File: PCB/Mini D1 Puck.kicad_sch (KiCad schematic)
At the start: 10 parts, among them M1 VI1, M2 VI2, M3 VI3, M4 VI4, Q1 2N2222, SW1 SW_SPDT

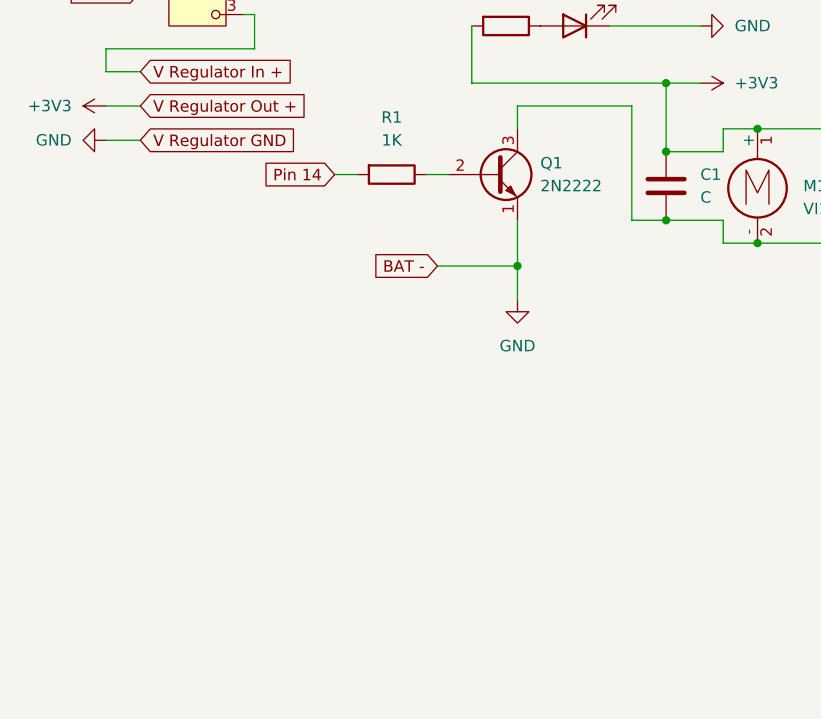
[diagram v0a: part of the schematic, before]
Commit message: Add voltage divider to schematic to measure battery level
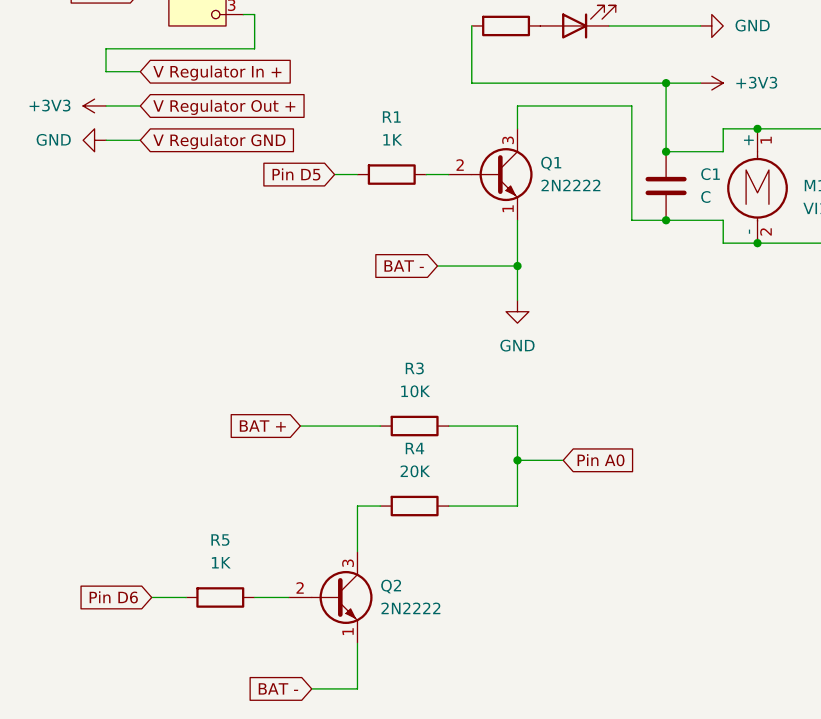
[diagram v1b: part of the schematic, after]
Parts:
- added Q2: 2N2222, symbol Transistor_BJT:Q_NPN_EBC
- added R3: 10K, symbol Device:R
- added R4: 20K, symbol Device:R
- added R5: 1K, symbol Device:R
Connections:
- net BAT +: now also R3.2
- net GND: now also Q2.1 (E)
- net Pin 14 renamed Pin D5
- new net: Q2.2 (B), R5.1
- new net: Q2.3 (C), R4.2
- new net Pin A0: R3.1, R4.1
- new net Pin D6: R5.2

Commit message: Ui WORK
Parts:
- C1: value C -> 200uF
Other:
- moved on the sheet: M1, M2, M3
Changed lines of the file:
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@@
-	)
-	(junction
-		(at 124.46 48.26)
-		(diameter 0)
-		(color 0 0 0 0)
-	)
-	(junction
-		(at 124.46 60.96)
-		(diameter 0)
-		(color 0 0 0 0)
 	)
 	(junction
@@
 	)
 	(junction
-		(at 99.06 48.26)
+		(at 125.73 60.96)
+		(diameter 0)
+		(color 0 0 0 0)
+	)
+	(junction
+		(at 114.3 60.96)
 		(diameter 0)
 		(color 0 0 0 0)
@@
 	)
 	(junction
-		(at 111.76 60.96)
+		(at 102.87 60.96)
 		(diameter 0)
 		(color 0 0 0 0)
 	)
 	(junction
-		(at 99.06 60.96)
+		(at 102.87 48.26)
+		(diameter 0)
+		(color 0 0 0 0)
+	)
+	(junction
+		(at 125.73 48.26)
 		(diameter 0)
 		(color 0 0 0 0)
@@
 	)
 	(junction
-		(at 111.76 48.26)
+		(at 114.3 48.26)
 		(diameter 0)
 		(color 0 0 0 0)
@@
 	(wire
 		(pts
+			(xy 102.87 60.96) (xy 114.3 60.96)
+		)
+		(stroke
+			(width 0)
+			(type default)
+		)
+	)
+	(wire
+		(pts
 			(xy 85.09 45.72) (xy 85.09 58.42)
 		)
@@
 	(wire
 		(pts
+			(xy 125.73 48.26) (xy 137.16 48.26)
+		)
+		(stroke
+			(width 0)
+			(type default)
+		)
+	)
+	(wire
+		(pts
 			(xy 72.39 81.28) (xy 72.39 85.09)
 		)
@@
 	(wire
 		(pts
-			(xy 111.76 60.96) (xy 124.46 60.96)
-		)
-		(stroke
-			(width 0)
-			(type default)
-		)
-	)
-	(wire
-		(pts
 			(xy 88.9 50.8) (xy 95.25 50.8)
 		)
@@
 	(wire
 		(pts
-			(xy 99.06 48.26) (xy 111.76 48.26)
+			(xy 114.3 48.26) (xy 125.73 48.26)
 		)
 		(stroke
@@
 	(wire
 		(pts
-			(xy 111.76 48.26) (xy 124.46 48.26)
-		)
-		(stroke
-			(width 0)
-			(type default)
-		)
-	)
-	(wire
-		(pts
 			(xy 54.61 110.49) (xy 49.53 110.49)
 		)
@@
 	(wire
 		(pts
-			(xy 124.46 60.96) (xy 137.16 60.96)
-		)
-		(stroke
-			(width 0)
-			(type default)
-		)
-	)
-	(wire
-		(pts
 			(xy 72.39 45.72) (xy 85.09 45.72)
 		)
@@
 	(wire
 		(pts
-			(xy 95.25 60.96) (xy 99.06 60.96)
+			(xy 95.25 60.96) (xy 102.87 60.96)
 		)
 		(stroke
@@
 	(wire
 		(pts
+			(xy 102.87 48.26) (xy 114.3 48.26)
+		)
+		(stroke
+			(width 0)
+			(type default)
+		)
+	)
+	(wire
+		(pts
 			(xy 26.67 39.37) (xy 26.67 41.91)
 		)
@@
 	(wire
 		(pts
+			(xy 125.73 60.96) (xy 137.16 60.96)
+		)
+		(stroke
+			(width 0)
+			(type default)
+		)
+	)
+	(wire
+		(pts
 			(xy 95.25 58.42) (xy 95.25 60.96)
 		)
@@
 	(wire
 		(pts
+			(xy 114.3 60.96) (xy 125.73 60.96)
+		)
+		(stroke
+			(width 0)
+			(type default)
+		)
+	)
+	(wire
+		(pts
 			(xy 64.77 81.28) (xy 72.39 81.28)
 		)
@@
 	(wire
 		(pts
-			(xy 124.46 48.26) (xy 137.16 48.26)
-		)
-		(stroke
-			(width 0)
-			(type default)
-		)
-	)
-	(wire
-		(pts
 			(xy 72.39 45.72) (xy 72.39 48.26)
 		)
@@
 	(wire
 		(pts
-			(xy 99.06 60.96) (xy 111.76 60.96)
-		)
-		(stroke
-			(width 0)
-			(type default)
-		)
-	)
-	(wire
-		(pts
 			(xy 82.55 36.83) (xy 92.71 36.83)
 		)
@@
 	(wire
 		(pts
-			(xy 95.25 48.26) (xy 99.06 48.26)
+			(xy 95.25 48.26) (xy 102.87 48.26)
 		)
 		(stroke
@@
 			)
 		)
-		(property "Value" "C"
+		(property "Value" "200uF"
 			(at 92.71 55.8799 0)
 			(effects
@@
 	(symbol
 		(lib_id "Motor:Motor_DC")
-		(at 111.76 53.34 0)
+		(at 114.3 53.34 0)
 		(unit 1)
 		(exclude_from_sim no)
@@
 		(fields_autoplaced yes)
 		(property "Reference" "M2"
-			(at 116.84 54.6099 0)
+			(at 119.38 54.6099 0)
 			(effects
 				(font
@@
 		)
 		(property "Value" "VI2"
-			(at 116.84 57.1499 0)
+			(at 119.38 57.1499 0)
 			(effects
 				(font
@@
 		)
 		(property "Footprint" ""
-			(at 111.76 55.626 0)
+			(at 114.3 55.626 0)
 			(effects
 				(font
@@
 		)
 		(property "Datasheet" "~"
-			(at 111.76 55.626 0)
+			(at 114.3 55.626 0)
 			(effects
 				(font
@@
 		)
 		(property "Description" "DC Motor"
-			(at 111.76 53.34 0)
+			(at 114.3 53.34 0)
 			(effects
 				(font
@@
 	(symbol
 		(lib_id "Motor:Motor_DC")
-		(at 124.46 53.34 0)
+		(at 125.73 53.34 0)
 		(unit 1)
 		(exclude_from_sim no)
@@
 		(fields_autoplaced yes)
 		(property "Reference" "M3"
-			(at 129.54 54.6099 0)
+			(at 130.81 54.6099 0)
 			(effects
 				(font
@@
 		)
 		(property "Value" "VI3"
-			(at 129.54 57.1499 0)
+			(at 130.81 57.1499 0)
 			(effects
 				(font
@@
 		)
 		(property "Footprint" ""
-			(at 124.46 55.626 0)
+			(at 125.73 55.626 0)
 			(effects
 				(font
@@
 		)
 		(property "Datasheet" "~"
-			(at 124.46 55.626 0)
+			(at 125.73 55.626 0)
 			(effects
 				(font
@@
 		)
 		(property "Description" "DC Motor"
-			(at 124.46 53.34 0)
+			(at 125.73 53.34 0)
 			(effects
 				(font
@@
 	(symbol
 		(lib_id "Motor:Motor_DC")
-		(at 99.06 53.34 0)
+		(at 102.87 53.34 0)
 		(unit 1)
 		(exclude_from_sim no)
@@
 		(fields_autoplaced yes)
 		(property "Reference" "M1"
-			(at 104.14 54.6099 0)
+			(at 107.95 54.6099 0)
 			(effects
 				(font
@@
 		)
 		(property "Value" "VI1"
-			(at 104.14 57.1499 0)
+			(at 107.95 57.1499 0)
 			(effects
 				(font
@@
 		)
 		(property "Footprint" ""
-			(at 99.06 55.626 0)
+			(at 102.87 55.626 0)
 			(effects
 				(font
@@
 		)
 		(property "Datasheet" "~"
-			(at 99.06 55.626 0)
+			(at 102.87 55.626 0)
 			(effects
 				(font
@@
 		)
 		(property "Description" "DC Motor"
-			(at 99.06 53.34 0)
-			(effects
-				(font
+			(at 102.87 53.34 0)
+			(effects
+				(font

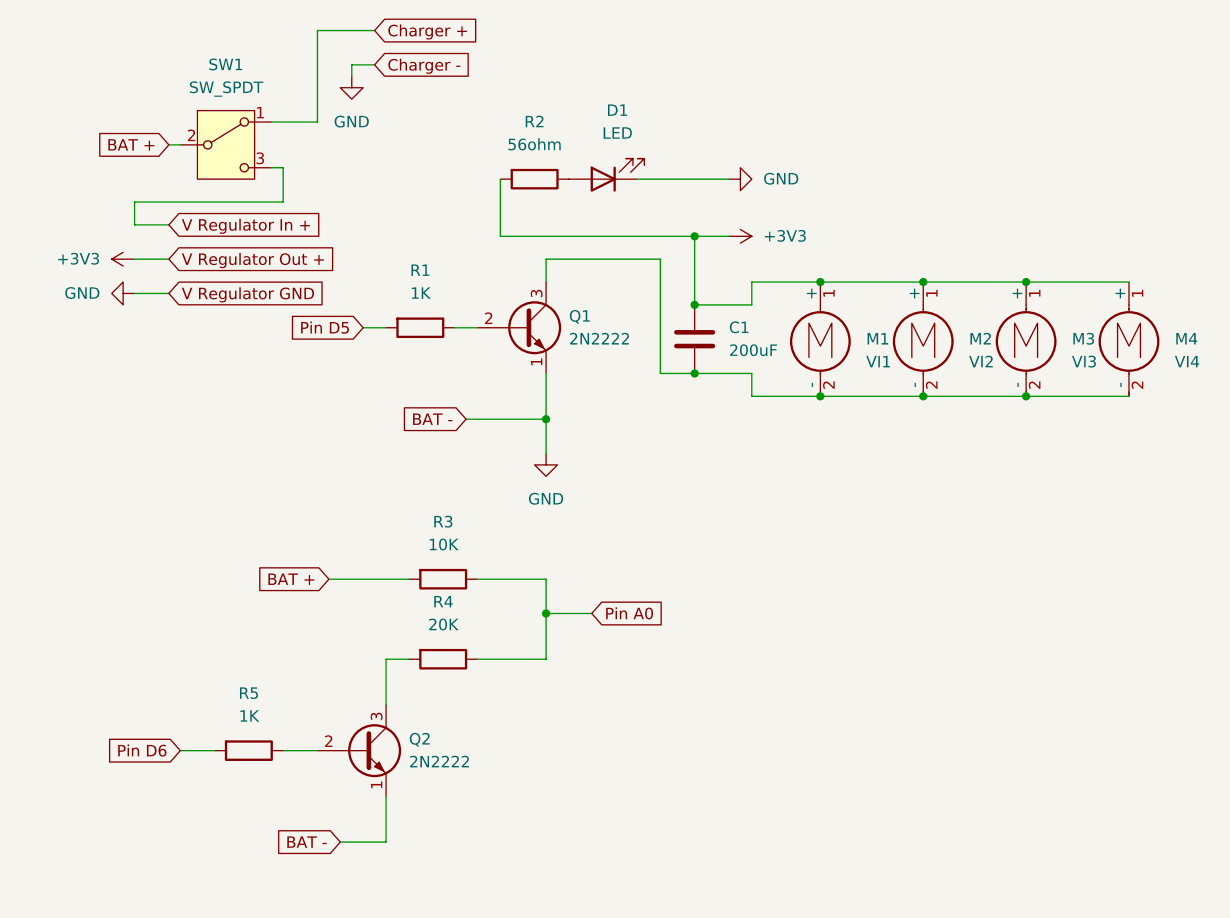
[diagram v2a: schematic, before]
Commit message: NHD Router App State/refactor, HP schematic rework
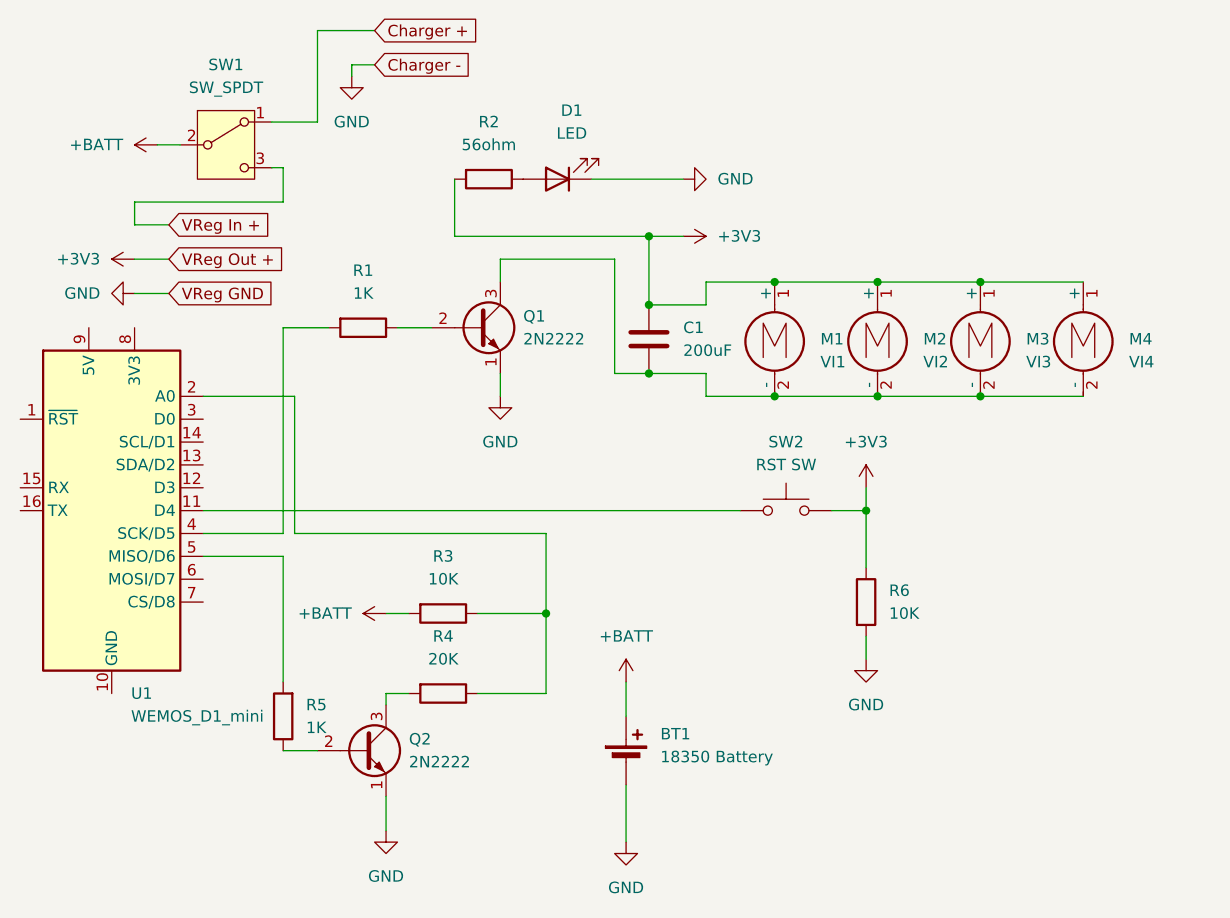
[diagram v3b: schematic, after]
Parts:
- added BT1: 18350 Battery, symbol Device:Battery_Cell
- added R6: 10K, symbol Device:R
- added SW2: RST SW, symbol Switch:SW_Push
- added U1: WEMOS_D1_mini, RF_Module:WEMOS_D1_mini_light, symbol RF_Module:WEMOS_D1_mini
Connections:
- net +3V3: now also R6.1, SW2.2
- net GND: now also BT1.2 (-), R6.2
- net BAT + renamed +BATT
- net +BATT: now also BT1.1 (+)
- net Pin A0: no longer names the net of R3.1, R4.1
- net Pin A0: now also U1.2 (A0)
- net Pin D5: no longer names the net of R1.2
- net Pin D5: now also U1.4 (SCK/D5)
- net Pin D6: no longer names the net of R5.2
- net Pin D6: now also U1.5 (MISO/D6)
- net V Regulator In + renamed VReg In +
- new net: SW2.1, U1.11 (D4)
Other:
- company: (none) -> Connor Oliver
- title: (none) -> NHD HapticPuck
- moved on the sheet: C1, D1, M1, M2, M3, M4, Q1, R1, R2, R3, R4, R5

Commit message: Kicad PCB
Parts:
- added J1: Regulator, symbol Connector:Conn_01x03_Socket
- added J2: Charger, symbol Connector:Conn_01x02_Socket
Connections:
- net +3V3: now also U1.8 (3V3), J1.2 (Pin_2)
- net GND: now also U1.10 (GND), J1.3 (Pin_3), J2.2 (Pin_2)
- net Charger +: no longer names the net of SW1.1 (A)
- net Charger +: now also J2.1 (Pin_1)
- net VReg In +: no longer names the net of SW1.3 (C)
- net VReg In +: now also J1.1 (Pin_1)
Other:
- moved on the sheet: SW1

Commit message: PCB fixes/reset button
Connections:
- net at SW2.1: now also U1.13 (SDA/D2); no longer U1.11 (D4)
- net at U1.14 (SCL/D1): now also R1.2
- net at U1.4 (SCK/D5): no longer R1.2
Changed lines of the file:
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@@
 	(wire
 		(pts
-			(xy 43.18 53.34) (xy 48.26 53.34)
-		)
-		(stroke
-			(width 0)
-			(type default)
-		)
-	)
-	(wire
-		(pts
-			(xy 43.18 53.34) (xy 43.18 76.2)
+			(xy 36.83 53.34) (xy 36.83 66.04)
 		)
 		(stroke
@@
 	(wire
 		(pts
+			(xy 39.37 73.66) (xy 39.37 68.58)
+		)
+		(stroke
+			(width 0)
+			(type default)
+		)
+	)
+	(wire
+		(pts
 			(xy 109.22 48.26) (xy 120.65 48.26)
 		)
@@
 	(wire
 		(pts
+			(xy 34.29 68.58) (xy 39.37 68.58)
+		)
+		(stroke
+			(width 0)
+			(type default)
+		)
+	)
+	(wire
+		(pts
+			(xy 36.83 53.34) (xy 48.26 53.34)
+		)
+		(stroke
+			(width 0)
+			(type default)
+		)
+	)
+	(wire
+		(pts
 			(xy 35.56 33.02) (xy 36.83 33.02)
 		)
@@
 	(wire
 		(pts
-			(xy 43.18 76.2) (xy 34.29 76.2)
-		)
-		(stroke
-			(width 0)
-			(type default)
-		)
-	)
-	(wire
-		(pts
 			(xy 36.83 33.02) (xy 36.83 35.56)
 		)
@@
 	(wire
 		(pts
+			(xy 36.83 66.04) (xy 34.29 66.04)
+		)
+		(stroke
+			(width 0)
+			(type default)
+		)
+	)
+	(wire
+		(pts
 			(xy 120.65 60.96) (xy 132.08 60.96)
 		)
@@
 	(wire
 		(pts
-			(xy 34.29 73.66) (xy 93.98 73.66)
-		)
-		(stroke
-			(width 0)
-			(type default)
-		)
-	)
-	(wire
-		(pts
 			(xy 83.82 50.8) (xy 83.82 43.18)
 		)
@@
 		)
 		(stroke
+			(width 0)
+			(type default)
+		)
+	)
+	(wire
+		(pts
+			(xy 93.98 73.66) (xy 39.37 73.66)
+		)
+		(stroke

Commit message: repo cleanup, readme bom
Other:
- company: Connor Oliver -> SkyeCA
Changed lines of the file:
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@@
 		(date "2025-04-30")
 		(rev "0.1")
-		(company "Connor Oliver")
+		(company "SkyeCA")
 	)
 	(junction

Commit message: Fix battery monitor circuit, voltage divider not properly grounded
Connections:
- net GND: now also R3.1, R4.1, U1.2 (A0)
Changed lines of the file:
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@@
+	)
+	(junction
+		(at 72.39 93.98)
+		(diameter 0)
+		(color 0 0 0 0)
 	)
 	(junction
@@
 		(pts
 			(xy 26.67 49.53) (xy 26.67 53.34)
+		)
+		(stroke
+			(width 0)
+			(type default)
+		)
+	)
+	(wire
+		(pts
+			(xy 72.39 93.98) (xy 72.39 97.79)
 		)
 		(stroke
@@
 					(unit 1)
 				)
+			)
+		)
+	)
+	(symbol
+		(lib_id "power:GND")
+		(at 72.39 97.79 0)
+		(unit 1)
+		(exclude_from_sim no)
+		(in_bom yes)
+		(on_board yes)
+		(dnp no)
+		(fields_autoplaced yes)
+		(property "Reference" "#PWR018"
+			(at 72.39 104.14 0)
+			(effects
+				(font
+					(size 1.27 1.27)
+				)
+				(hide yes)
+			)
+		)
+		(property "Value" "GND"
+			(at 72.39 102.87 0)
+			(effects
+				(font
+					(size 1.27 1.27)
+				)
+			)
+		)
+		(property "Footprint" ""
+			(at 72.39 97.79 0)
+			(effects
+				(font
+					(size 1.27 1.27)
+				)
+				(hide yes)
+			)
+		)
+		(property "Datasheet" ""
+			(at 72.39 97.79 0)
+			(effects
+				(font
+					(size 1.27 1.27)
+				)
+				(hide yes)
+			)
+		)
+		(property "Description" "Power symbol creates a global label with name \"GND\" , ground"
+			(at 72.39 97.79 0)
+			(effects
+				(font
+					(size 1.27 1.27)
+				)
+				(hide yes)
+			)
+		)
+		(pin "1"
+		)
+		(instances
+			(project "Mini D1 Puck"
+				(path "/bd8e677d-9a0d-480d-b73d-a24a4e82a69f"
+					(reference "#PWR018")
+					(unit 1)
+				)
